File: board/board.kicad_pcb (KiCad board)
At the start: 2 copper layers, 45 x 13 mm, 27 parts, among them J1 003_power, J2 Conn_01x02_Male, J3 022_battery_cells, Q1 Q_PNP_BCEC, Q2 Q_PNP_BCEC, U1 DS2711E+

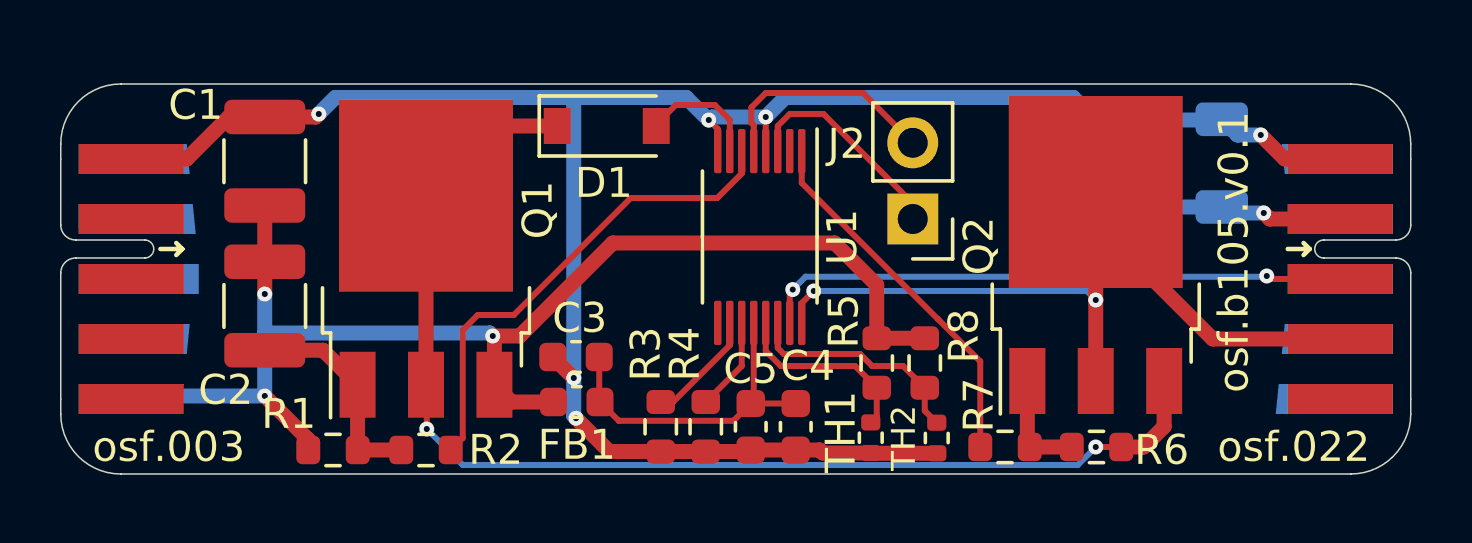
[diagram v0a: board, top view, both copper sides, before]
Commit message: fixed missing connection
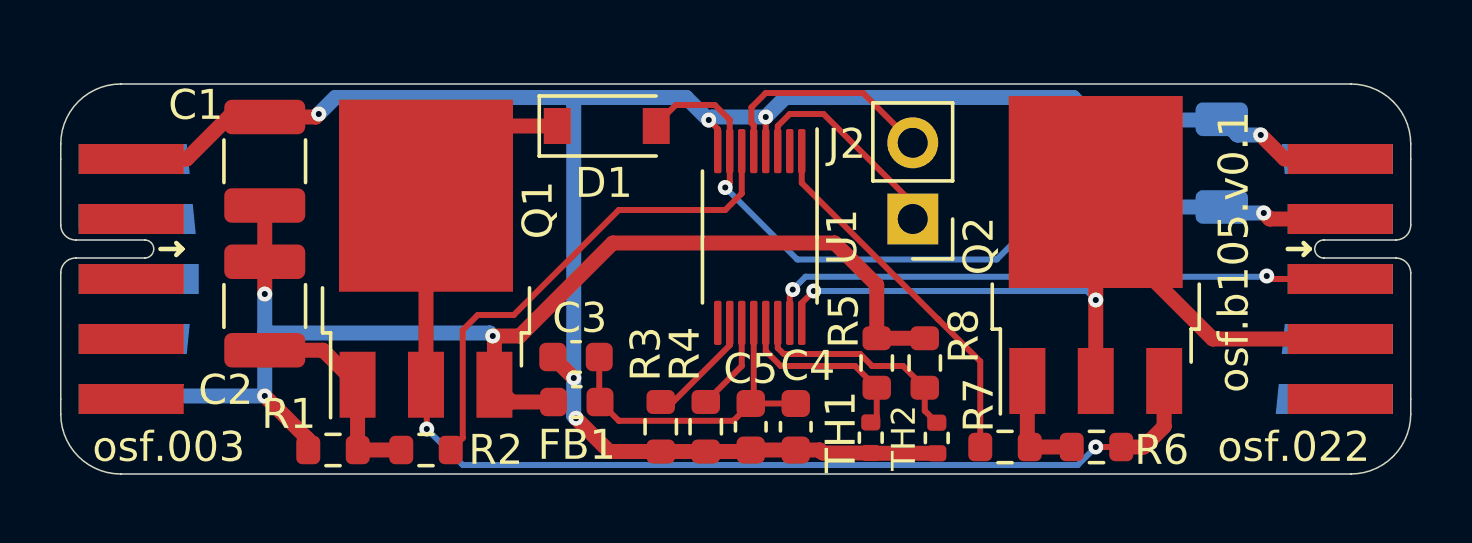
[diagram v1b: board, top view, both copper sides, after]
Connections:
- D1 pad 2: Net-(D1-Pad2) -> /charger/BTL
- U1 pad 7: Net-(D1-Pad2) -> /charger/BTL
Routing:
- net /charger/BTL: track 9.04 -> 28.9 mm, vias 1 -> 2
- net Net-(D1-Pad2): track 4.01 -> 0.00 mm
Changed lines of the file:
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@@
   (net 27 "/charger/LED1")
   (net 28 "/charger/LED2")
-  (net 29 "Net-(D1-Pad2)")
-  (net 30 "unconnected-(U1-Pad9)")
+  (net 29 "unconnected-(U1-Pad9)")
   (footprint "Resistor_SMD:R_0603_1608Metric" (layer "F.Cu")
     (at 167.2 99.3 90)
@@
       (net 20 "Net-(R2-Pad2)") (pinfunction "CSOUT") (pintype "passive"))
     (pad "7" smd roundrect (at -2.8625 1 270) (size 1.475 0.25) (layers "F.Cu" "F.Paste" "F.Mask") (roundrect_rratio 0.25)
-      (net 29 "Net-(D1-Pad2)") (pinfunction "VN1") (pintype "passive"))
+      (net 3 "/charger/BTL") (pinfunction "VN1") (pintype "passive"))
     (pad "8" smd roundrect (at -2.8625 1.4 270) (size 1.475 0.25) (layers "F.Cu" "F.Paste" "F.Mask") (roundrect_rratio 0.25)
       (net 2 "GND") (pinfunction "VN0") (pintype "passive"))
     (pad "9" smd roundrect (at 2.8625 1.4 270) (size 1.475 0.25) (layers "F.Cu" "F.Paste" "F.Mask") (roundrect_rratio 0.25)
-      (net 30 "unconnected-(U1-Pad9)") (pinfunction "DMSEL") (pintype "passive+no_connect"))
+      (net 29 "unconnected-(U1-Pad9)") (pinfunction "DMSEL") (pintype "passive+no_connect"))
     (pad "10" smd roundrect (at 2.8625 1 270) (size 1.475 0.25) (layers "F.Cu" "F.Paste" "F.Mask") (roundrect_rratio 0.25)
       (net 21 "Net-(R3-Pad2)") (pinfunction "CTST") (pintype "passive"))
@@
       (net 18 "Net-(D1-Pad1)") (pinfunction "K") (pintype "passive"))
     (pad "2" smd rect (at 1.65 0) (size 0.9 1.2) (layers "F.Cu" "F.Paste" "F.Mask")
-      (net 29 "Net-(D1-Pad2)") (pinfunction "A") (pintype "passive"))
+      (net 3 "/charger/BTL") (pinfunction "A") (pintype "passive"))
     (model "${KICAD6_3DMODEL_DIR}/Diode_SMD.3dshapes/D_SOD-123.wrl"
       (offset (xyz 0 0 0))
@@
   (segment (start 179.225 91.7) (end 178.7 91.175) (width 0.5) (layer "B.Cu") (net 2))
   (segment (start 160.85 90.45) (end 156.95 90.45) (width 0.5) (layer "B.Cu") (net 2))
+  (segment (start 162.3 93.3) (end 162.15 93.45) (width 0.2) (layer "F.Cu") (net 3))
   (segment (start 182.65 94.5) (end 180.3 94.5) (width 0.5) (layer "F.Cu") (net 3))
+  (segment (start 162.3 91.2) (end 161.8 90.7) (width 0.2) (layer "F.Cu") (net 3))
+  (segment (start 160.5 90.7) (end 159.85 91.35) (width 0.2) (layer "F.Cu") (net 3))
+  (segment (start 159.85 91.35) (end 159.85 91.4) (width 0.2) (layer "F.Cu") (net 3))
+  (segment (start 162.3 92.2375) (end 162.3 91.2) (width 0.2) (layer "F.Cu") (net 3))
+  (segment (start 161.8 90.7) (end 160.5 90.7) (width 0.2) (layer "F.Cu") (net 3))
   (segment (start 180.3 94.5) (end 180.1 94.3) (width 0.5) (layer "F.Cu") (net 3))
+  (segment (start 162.3 92.2375) (end 162.3 93.3) (width 0.2) (layer "F.Cu") (net 3))
   (via (at 180.1 94.3) (size 0.5) (drill 0.2) (layers "F.Cu" "B.Cu") (net 3))
+  (via (at 162.15 93.45) (size 0.5) (drill 0.2) (layers "F.Cu" "B.Cu") (net 3))
+  (segment (start 171.2 95.85) (end 174.4 92.65) (width 0.2) (layer "B.Cu") (net 3))
   (segment (start 176.4 94.125) (end 175.875 94.125) (width 0.5) (layer "B.Cu") (net 3))
   (segment (start 176.425 94.1) (end 176.4 94.125) (width 0.5) (layer "B.Cu") (net 3))
@@
   (segment (start 178.7 94.1) (end 176.425 94.1) (width 0.5) (layer "B.Cu") (net 3))
   (segment (start 175.875 94.125) (end 174.4 92.65) (width 0.5) (layer "B.Cu") (net 3))
+  (segment (start 162.15 93.45) (end 164.55 95.85) (width 0.2) (layer "B.Cu") (net 3))
+  (segment (start 164.55 95.85) (end 171.2 95.85) (width 0.2) (layer "B.Cu") (net 3))
   (segment (start 178.9 94.3) (end 178.7 94.1) (width 0.5) (layer "B.Cu") (net 3))
   (segment (start 165.8 95.3) (end 158.4 95.3) (width 0.5) (layer "F.Cu") (net 12))
@@
   (segment (start 172.22 102.02) (end 172.3 102.1) (width 0.5) (layer "F.Cu") (net 19))
   (segment (start 172.22 99.9) (end 172.22 102.02) (width 0.5) (layer "F.Cu") (net 19))
+  (segment (start 162.7 93.65) (end 162.15 94.2) (width 0.2) (layer "F.Cu") (net 20))
+  (segment (start 162.7 92.2375) (end 162.7 93.65) (width 0.2) (layer "F.Cu") (net 20))
+  (segment (start 153.4 98.2) (end 153.4 101.8) (width 0.2) (layer "F.Cu") (net 20))
+  (segment (start 158.6 94.2) (end 155.1 97.7) (width 0.2) (layer "F.Cu") (net 20))
   (segment (start 155.1 97.7) (end 153.9 97.7) (width 0.2) (layer "F.Cu") (net 20))
-  (segment (start 153.4 98.2) (end 153.4 101.8) (width 0.2) (layer "F.Cu") (net 20))
   (segment (start 153.9 97.7) (end 153.4 98.2) (width 0.2) (layer "F.Cu") (net 20))
-  (segment (start 159 93.8) (end 155.1 97.7) (width 0.2) (layer "F.Cu") (net 20))
+  (segment (start 162.15 94.2) (end 158.6 94.2) (width 0.2) (layer "F.Cu") (net 20))
   (segment (start 153.4 101.8) (end 153 102.2) (width 0.2) (layer "F.Cu") (net 20))
-  (segment (start 162.7 92.2375) (end 162.7 92.984415) (width 0.2) (layer "F.Cu") (net 20))
-  (segment (start 161.884415 93.8) (end 159 93.8) (width 0.2) (layer "F.Cu") (net 20))
-  (segment (start 162.7 92.984415) (end 161.884415 93.8) (width 0.2) (layer "F.Cu") (net 20))
   (segment (start 162.3 98.709415) (end 160.409415 100.6) (width 0.2) (layer "F.Cu") (net 21))
   (segment (start 162.3 97.9625) (end 162.3 98.709415) (width 0.2) (layer "F.Cu") (net 21))
@@
   (segment (start 163.1 92.2375) (end 163.1 91.37458) (width 0.2) (layer "F.Cu") (net 28))
   (segment (start 163.5 90.3) (end 166.74 90.3) (width 0.2) (layer "F.Cu") (net 28))
-  (segment (start 162.3 91.2) (end 161.8 90.7) (width 0.2) (layer "F.Cu") (net 29))
-  (segment (start 160.5 90.7) (end 159.85 91.35) (width 0.2) (layer "F.Cu") (net 29))
-  (segment (start 159.85 91.35) (end 159.85 91.4) (width 0.2) (layer "F.Cu") (net 29))
-  (segment (start 162.3 92.2375) (end 162.3 91.2) (width 0.2) (layer "F.Cu") (net 29))
-  (segment (start 161.8 90.7) (end 160.5 90.7) (width 0.2) (layer "F.Cu") (net 29))
 )

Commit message: fixed footprint
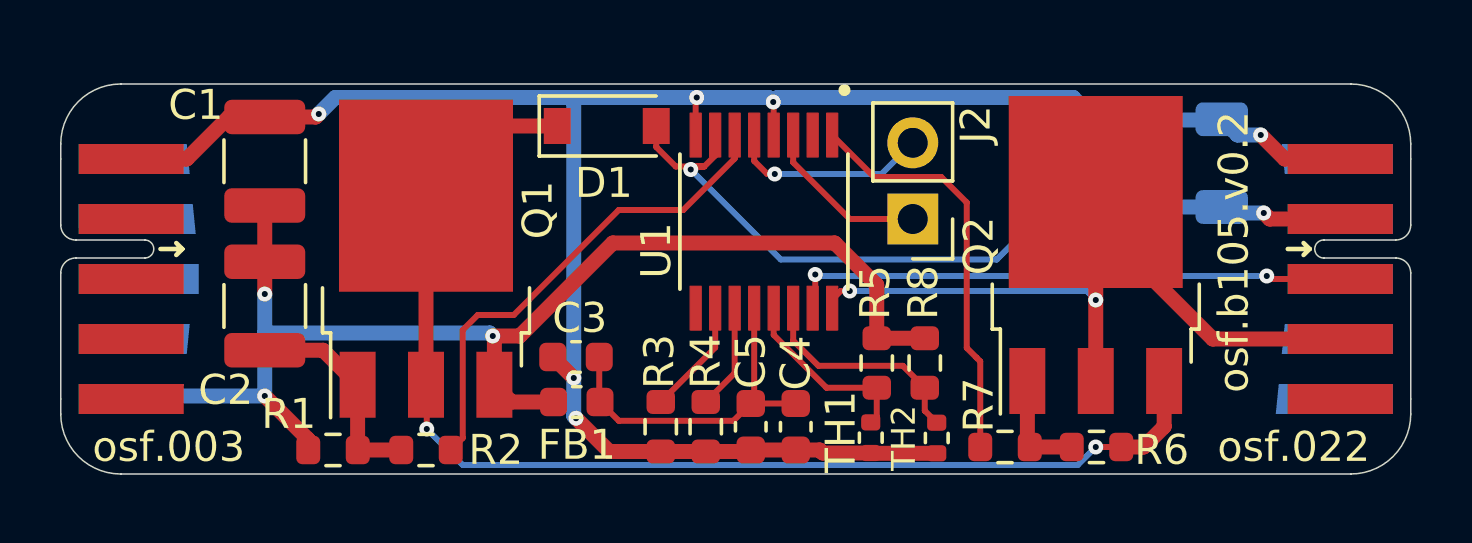
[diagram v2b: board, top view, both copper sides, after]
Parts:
- U1: footprint Package_SO:TSSOP-16_4.4x3.6mm_P0.4mm -> b105:SOP65P640X110-16N
- moved U1 0.53 mm to (163.4, 94.6)
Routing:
- net /charger/BTH: track 27.8 -> 26.4 mm
- net Net-(R7-Pad1): track 12.3 -> 13.8 mm
- net /charger/LED1: track 6.73 -> 5.68 mm
- net /charger/LED2: track 7.75 -> 6.76 mm, vias 0 -> 1
- net /charger/BTM: track 19.6 -> 18.7 mm
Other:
- board text added: "osf.b105.v0.2"
- board text removed: "osf.b105.v0.1"

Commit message: added missing limmiting resistor to protect zener diode
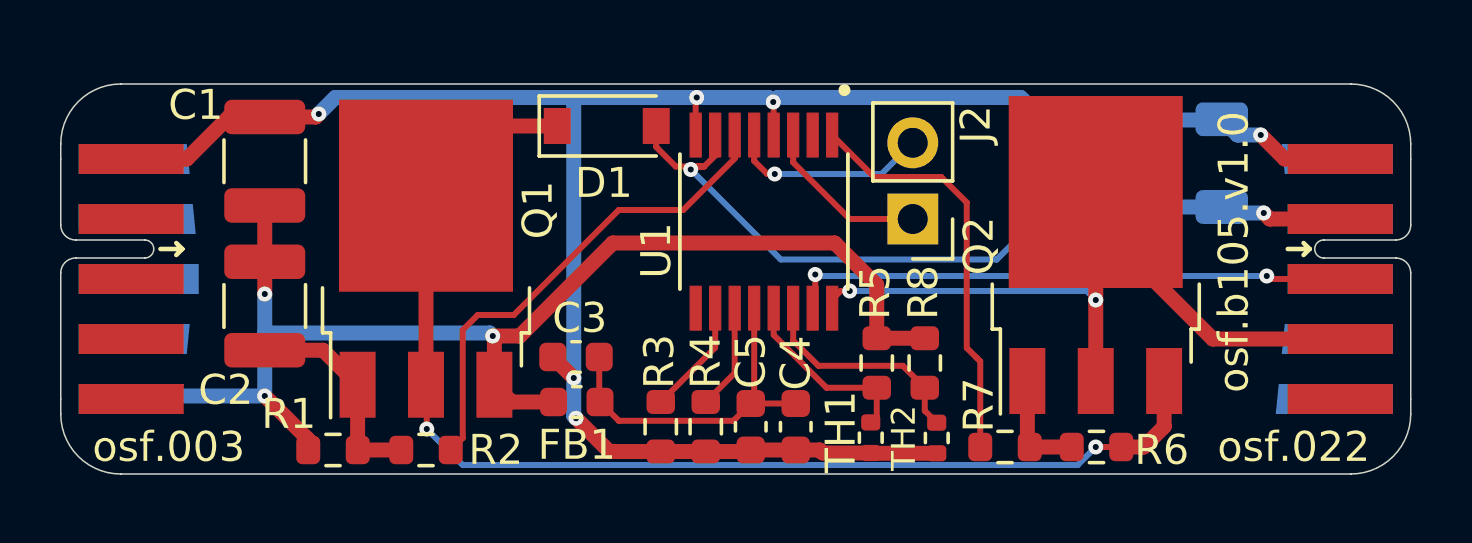
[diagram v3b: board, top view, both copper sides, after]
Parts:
- added R11: 10R, Resistor_SMD:R_0603_1608Metric, B.Cu at (174.3, 93.5)
- moved C6 1.75 mm to (172.7, 91.9)
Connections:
- C6 pad 1: /charger/BTL -> /charger/VN1
- D1 pad 2: /charger/BTL -> /charger/VN1
- U1 pad 7: /charger/BTL -> /charger/VN1
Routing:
- net /charger/VN1: track 0.00 -> 21.2 mm, vias 0 -> 1
- net /charger/BTL: track 29.3 -> 8.56 mm, vias 2 -> 1
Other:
- board text added: "osf.b105.v1.0"
- board text removed: "osf.b105.v0.2"
